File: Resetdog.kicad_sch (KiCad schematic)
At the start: 20 parts, among them U14 MC14541BD, U15 MC74HC4538ADG, U20 74LVC1G17

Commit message: Update the manufacturer part number for some of components to be compatible with avaiable parts in the JLC parts database
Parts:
- C80: JLCPCB Part # C5969198 -> C338087; Manufacturer_Part_Number CL10A475KP8NNWC -> CGA3E1X5R0J475KT0Y0E
- C81, C82: JLCPCB Part # C307479 -> C342956; Manufacturer_Part_Number CL10B105KA8NFNC -> CGA3E1X7R1V105KT000N
- C83: JLCPCB Part # (none) -> C129629; Manufacturer_Part_Number CL10B473KB8VPJC -> C0603C473K5RACAUTO
- C84, C85: JLCPCB Part # C1591 -> C129621; Manufacturer_Part_Number CL10B104KB8NNNC -> C0603C104K5RACAUTO
- D9: Manufacturer_Part_Number BAS70H,115 -> BAS70H,115
- U15: JLCPCB Part # C7292 -> C233613
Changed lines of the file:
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@@
       (effects (font (size 1.27 1.27)) hide)
     )
-    (property "JLCPCB Part #" "C1591" (id 4) (at 103.632 60.706 0)
-      (effects (font (size 1.27 1.27)) hide)
-    )
-    (property "Manufacturer_Part_Number" "CL10B104KB8NNNC " (id 5) (at 103.632 60.706 0)
+    (property "JLCPCB Part #" "C129621" (id 4) (at 103.632 60.706 0)
+      (effects (font (size 1.27 1.27)) hide)
+    )
+    (property "Manufacturer_Part_Number" "C0603C104K5RACAUTO" (id 5) (at 103.632 60.706 0)
       (effects (font (size 1.27 1.27)) hide)
     )
@@
       (effects (font (size 1.27 1.27)) hide)
     )
-    (property "JLCPCB Part #" "C7292" (id 5) (at 154.94 90.17 0)
+    (property "JLCPCB Part #" "C233613" (id 5) (at 154.94 90.17 0)
       (effects (font (size 1.27 1.27)) hide)
     )
@@
       (effects (font (size 1.27 1.27)) hide)
     )
-    (property "JLCPCB Part #" "C307479" (id 4) (at 134.62 123.19 0)
-      (effects (font (size 1.27 1.27)) hide)
-    )
-    (property "Manufacturer_Part_Number" "CL10B105KA8NFNC " (id 5) (at 134.62 123.19 0)
+    (property "JLCPCB Part #" "C342956" (id 4) (at 134.62 123.19 0)
+      (effects (font (size 1.27 1.27)) hide)
+    )
+    (property "Manufacturer_Part_Number" "CGA3E1X7R1V105KT000N" (id 5) (at 134.62 123.19 0)
       (effects (font (size 1.27 1.27)) hide)
     )
@@
       (effects (font (size 1.27 1.27)) hide)
     )
-    (property "JLCPCB Part #" "C1591" (id 4) (at 177.038 56.642 0)
-      (effects (font (size 1.27 1.27)) hide)
-    )
-    (property "Manufacturer_Part_Number" "CL10B104KB8NNNC " (id 5) (at 177.038 56.642 0)
+    (property "JLCPCB Part #" "C129621" (id 4) (at 177.038 56.642 0)
+      (effects (font (size 1.27 1.27)) hide)
+    )
+    (property "Manufacturer_Part_Number" "C0603C104K5RACAUTO" (id 5) (at 177.038 56.642 0)
       (effects (font (size 1.27 1.27)) hide)
     )
@@
       (effects (font (size 1.27 1.27)) hide)
     )
-    (property "Manufacturer_Part_Number" "BAS70H,115 " (id 4) (at 120.65 93.98 90)
+    (property "Manufacturer_Part_Number" "BAS70H,115" (id 4) (at 120.65 93.98 90)
       (effects (font (size 1.27 1.27)) hide)
     )
@@
       (effects (font (size 1.27 1.27)) hide)
     )
-    (property "Manufacturer_Part_Number" "CL10B473KB8VPJC " (id 4) (at 40.64 130.81 0)
+    (property "Manufacturer_Part_Number" "C0603C473K5RACAUTO" (id 4) (at 40.64 130.81 0)
+      (effects (font (size 1.27 1.27)) hide)
+    )
+    (property "JLCPCB Part #" "C129629" (id 5) (at 40.64 130.81 0)
       (effects (font (size 1.27 1.27)) hide)
     )
@@
       (effects (font (size 1.27 1.27)) hide)
     )
-    (property "JLCPCB Part #" "C5969198" (id 4) (at 71.12 77.47 0)
-      (effects (font (size 1.27 1.27)) hide)
-    )
-    (property "Manufacturer_Part_Number" "CL10A475KP8NNWC " (id 5) (at 71.12 77.47 0)
+    (property "JLCPCB Part #" "C338087" (id 4) (at 71.12 77.47 0)
+      (effects (font (size 1.27 1.27)) hide)
+    )
+    (property "Manufacturer_Part_Number" "CGA3E1X5R0J475KT0Y0E" (id 5) (at 71.12 77.47 0)
       (effects (font (size 1.27 1.27)) hide)
     )
@@
       (effects (font (size 1.27 1.27)) hide)
     )
-    (property "JLCPCB Part #" "C307479" (id 4) (at 127 101.6 0)
-      (effects (font (size 1.27 1.27)) hide)
-    )
-    (property "Manufacturer_Part_Number" "CL10B105KA8NFNC " (id 5) (at 127 101.6 0)
-      (effects (font (size 1.27 1.27)) hide)
-    )
+    (property "JLCPCB Part #" "C342956" (id 4) (at 127 101.6 0)
+      (effects (font (size 1.27 1.27)) hide)
+    )
+    (property "Manufacturer_Part_Number" "CGA3E1X7R1V105KT000N" (id 5) (at 127 101.6 0)
+      (effects (font (size 1.27 1.27)) hide)
+    )

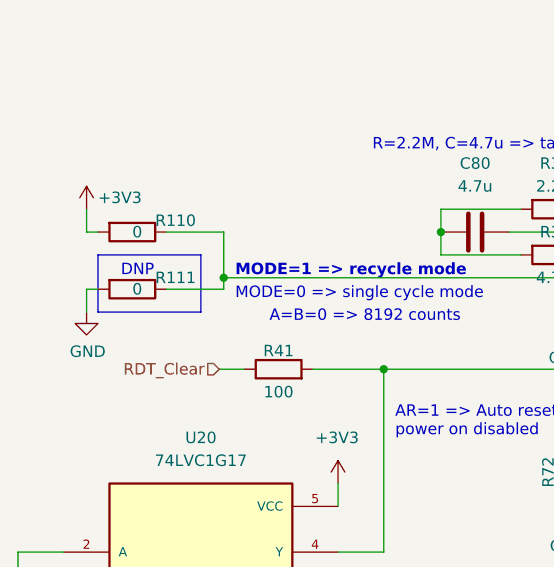
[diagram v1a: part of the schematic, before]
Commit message: Update kicad files to v9.0 from v6.0
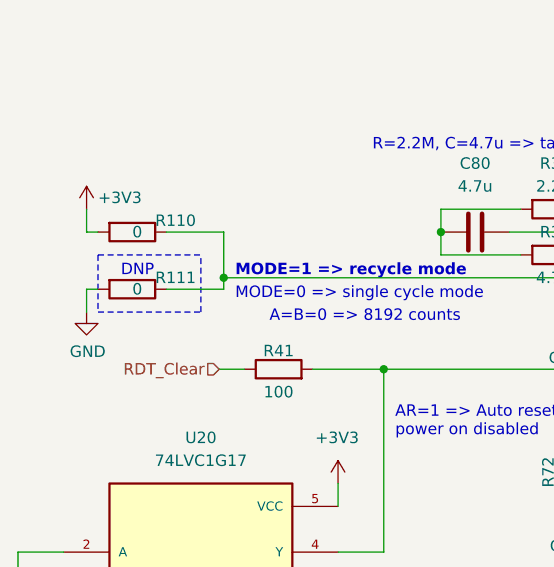
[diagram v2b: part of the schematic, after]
